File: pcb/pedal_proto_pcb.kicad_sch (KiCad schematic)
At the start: 18 parts, among them J1 100k_pot_1, J10 100k_pot_2, J11 250k_pot_1, J12 250k_pot_2, J13 stomp_b, J14 stomp_a, J15 stomp_c, J16 switch, J17 LED, J18 LED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

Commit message: feat: pcb done
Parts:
- removed J10: 100k_pot_2, symbol Connector:Conn_01x03_Socket
- removed J11: 250k_pot_1, symbol Connector:Conn_01x03_Socket
- removed J12: 250k_pot_2, symbol Connector:Conn_01x03_Socket
- removed J13: stomp_b, symbol Connector:Conn_01x03_Socket
- removed J14: stomp_a, symbol Connector:Conn_01x03_Socket
- removed J15: stomp_c, symbol Connector:Conn_01x03_Socket
- removed J16: switch, symbol Connector:Conn_01x03_Socket
- removed J9: 100k_pot_1, symbol Connector:Conn_01x03_Socket
- added J10: 100k_pot_1_B, Connector_PinHeader_2.54mm:PinHeader_1x02_P2.54mm_Vertical, symbol Connector:Conn_01x02_Socket
- added J11: 100k_pot_1_C, Connector_PinHeader_2.54mm:PinHeader_1x02_P2.54mm_Vertical, symbol Connector:Conn_01x02_Socket
- added J12: 100k_pot_2_A, Connector_PinHeader_2.54mm:PinHeader_1x02_P2.54mm_Vertical, symbol Connector:Conn_01x02_Socket
- added J13: 100k_pot_2_B, Connector_PinHeader_2.54mm:PinHeader_1x02_P2.54mm_Vertical, symbol Connector:Conn_01x02_Socket
- added J14: 100k_pot_2_C, Connector_PinHeader_2.54mm:PinHeader_1x02_P2.54mm_Vertical, symbol Connector:Conn_01x02_Socket
- added J15: 250k_pot_1_A, Connector_PinHeader_2.54mm:PinHeader_1x02_P2.54mm_Vertical, symbol Connector:Conn_01x02_Socket
- added J16: 250k_pot_1_B, Connector_PinHeader_2.54mm:PinHeader_1x02_P2.54mm_Vertical, symbol Connector:Conn_01x02_Socket
- added J19: 250k_pot_2_B, Connector_PinHeader_2.54mm:PinHeader_1x02_P2.54mm_Vertical, symbol Connector:Conn_01x02_Socket
- added J20: 250k_pot_2_C, Connector_PinHeader_2.54mm:PinHeader_1x02_P2.54mm_Vertical, symbol Connector:Conn_01x02_Socket
- added J21: stomp_1_A, Connector_PinHeader_2.54mm:PinHeader_1x02_P2.54mm_Vertical, symbol Connector:Conn_01x02_Socket
- added J22: stomp_1_B, Connector_PinHeader_2.54mm:PinHeader_1x02_P2.54mm_Vertical, symbol Connector:Conn_01x02_Socket
- added J23: stomp_1_C, Connector_PinHeader_2.54mm:PinHeader_1x02_P2.54mm_Vertical, symbol Connector:Conn_01x02_Socket
- added J24: stomp_2_A, Connector_PinHeader_2.54mm:PinHeader_1x02_P2.54mm_Vertical, symbol Connector:Conn_01x02_Socket
- added J25: stomp_2_B, Connector_PinHeader_2.54mm:PinHeader_1x02_P2.54mm_Vertical, symbol Connector:Conn_01x02_Socket
- added J26, J29: stomp_2_C, Connector_PinHeader_2.54mm:PinHeader_1x02_P2.54mm_Vertical, symbol Connector:Conn_01x02_Socket
- added J27: stomp_3_A, Connector_PinHeader_2.54mm:PinHeader_1x02_P2.54mm_Vertical, symbol Connector:Conn_01x02_Socket
- added J28: stomp_3_B, Connector_PinHeader_2.54mm:PinHeader_1x02_P2.54mm_Vertical, symbol Connector:Conn_01x02_Socket
- added J30: switch_A, Connector_PinHeader_2.54mm:PinHeader_1x02_P2.54mm_Vertical, symbol Connector:Conn_01x02_Socket
- added J31: switch_B, Connector_PinHeader_2.54mm:PinHeader_1x02_P2.54mm_Vertical, symbol Connector:Conn_01x02_Socket
- added J32: switch_C, Connector_PinHeader_2.54mm:PinHeader_1x02_P2.54mm_Vertical, symbol Connector:Conn_01x02_Socket
- added J33: GND, Connector_PinHeader_2.54mm:PinHeader_1x02_P2.54mm_Vertical, symbol Connector:Conn_01x02_Socket
- added J34: VDD, Connector_PinHeader_2.54mm:PinHeader_1x02_P2.54mm_Vertical, symbol Connector:Conn_01x02_Socket
- added J35: LED-, Connector_PinHeader_2.54mm:PinHeader_1x02_P2.54mm_Vertical, symbol Connector:Conn_01x02_Socket
- added J36: LED+, Connector_PinHeader_2.54mm:PinHeader_1x02_P2.54mm_Vertical, symbol Connector:Conn_01x02_Socket
- added J9: 100k_pot_1_A, Connector_PinHeader_2.54mm:PinHeader_1x02_P2.54mm_Vertical, symbol Connector:Conn_01x02_Socket
- J1, J2, J3, J4, J6: footprint (none) -> Connector_PinHeader_2.54mm:PinHeader_1x04_P2.54mm_Vertical
- J17: value LED -> 250k_pot_1_C; footprint (none) -> Connector_PinHeader_2.54mm:PinHeader_1x02_P2.54mm_Vertical
- J18: value LED -> 250k_pot_2_A; footprint (none) -> Connector_PinHeader_2.54mm:PinHeader_1x02_P2.54mm_Vertical
- J5: footprint (none) -> Connector_PinHeader_2.54mm:PinHeader_1x10_P2.54mm_Vertical
- J7, J8: footprint (none) -> Connector_PinHeader_2.54mm:PinHeader_1x02_P2.54mm_Vertical
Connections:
- net 0: now also J33.1 (Pin_1), J33.2 (Pin_2); no longer J18.1 (Pin_1)
- net VDD: now also J34.1 (Pin_1), J34.2 (Pin_2); no longer J18.2 (Pin_2)
- net at J6.2 (Pin_2): now also J30.1 (Pin_1), J30.2 (Pin_2)
- net at J6.3 (Pin_3): now also J31.1 (Pin_1), J31.2 (Pin_2)
- net at J6.4 (Pin_4): now also J32.1 (Pin_1), J32.2 (Pin_2)
- net at J5.5 (Pin_5): now also J24.1 (Pin_1), J24.2 (Pin_2)
- net at J5.6 (Pin_6): now also J25.1 (Pin_1), J25.2 (Pin_2)
- net at J5.7 (Pin_7): now also J26.1 (Pin_1), J26.2 (Pin_2)
- net at J2.2 (Pin_2): now also J12.1 (Pin_1), J12.2 (Pin_2)
- net at J2.3 (Pin_3): now also J13.1 (Pin_1), J13.2 (Pin_2)
- net at J2.4 (Pin_4): now also J14.1 (Pin_1), J14.2 (Pin_2)
- net at J5.10 (Pin_10): now also J29.1 (Pin_1), J29.2 (Pin_2)
- net at J5.2 (Pin_2): now also J21.1 (Pin_1), J21.2 (Pin_2)
- net at J5.3 (Pin_3): now also J22.1 (Pin_1), J22.2 (Pin_2)
- net at J5.4 (Pin_4): now also J23.1 (Pin_1), J23.2 (Pin_2)
- net at J5.8 (Pin_8): now also J27.1 (Pin_1), J27.2 (Pin_2)
- net at J5.9 (Pin_9): now also J28.1 (Pin_1), J28.2 (Pin_2)
- net at J1.2 (Pin_2): now also J9.1 (Pin_1), J9.2 (Pin_2)
- net at J1.3 (Pin_3): now also J10.1 (Pin_1), J10.2 (Pin_2)
- net at J1.4 (Pin_4): now also J11.1 (Pin_1), J11.2 (Pin_2)
- net at J4.2 (Pin_2): now also J18.1 (Pin_1), J18.2 (Pin_2)
- net at J4.3 (Pin_3): now also J19.1 (Pin_1), J19.2 (Pin_2)
- net at J4.4 (Pin_4): now also J20.1 (Pin_1), J20.2 (Pin_2)
- net at J3.2 (Pin_2): now also J15.1 (Pin_1), J15.2 (Pin_2)
- net at J3.3 (Pin_3): now also J16.1 (Pin_1), J16.2 (Pin_2)
- net at J3.4 (Pin_4): now also J17.1 (Pin_1), J17.2 (Pin_2)
- net at J8.1 (Pin_1): now also J35.1 (Pin_1), J35.2 (Pin_2); no longer J17.1 (Pin_1)
- net at J8.2 (Pin_2): now also J36.1 (Pin_1), J36.2 (Pin_2); no longer J17.2 (Pin_2)
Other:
- moved on the sheet: J1, J2, J3, J4, J5, J6, J7, J8

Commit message: feat: updated pcb
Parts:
- removed J1: 100k_pot_1, Connector_PinHeader_2.54mm:PinHeader_1x04_P2.54mm_Vertical, symbol Connector:Conn_01x04_Socket
- removed J2: 100k_pot_2, Connector_PinHeader_2.54mm:PinHeader_1x04_P2.54mm_Vertical, symbol Connector:Conn_01x04_Socket
- removed J3: 250k_pot_1, Connector_PinHeader_2.54mm:PinHeader_1x04_P2.54mm_Vertical, symbol Connector:Conn_01x04_Socket
- removed J4: 250k_pot_2, Connector_PinHeader_2.54mm:PinHeader_1x04_P2.54mm_Vertical, symbol Connector:Conn_01x04_Socket
- removed J5: stomp, Connector_PinHeader_2.54mm:PinHeader_1x10_P2.54mm_Vertical, symbol Connector:Conn_01x10_Socket
- removed J6: switch, Connector_PinHeader_2.54mm:PinHeader_1x04_P2.54mm_Vertical, symbol Connector:Conn_01x04_Socket
- removed J7: power, Connector_PinHeader_2.54mm:PinHeader_1x02_P2.54mm_Vertical, symbol Connector:Conn_01x02_Socket
- removed J8: LED, Connector_PinHeader_2.54mm:PinHeader_1x02_P2.54mm_Vertical, symbol Connector:Conn_01x02_Socket
- added D1: LED, LED_THT:LED_D4.0mm, symbol Device:LED
- added J1, J2, J3, J37, J4, J8: GND, Connector_PinHeader_2.54mm:PinHeader_1x01_P2.54mm_Vertical, symbol Connector:Conn_01x01_Socket
- added J38: input, Connector_PinHeader_2.54mm:PinHeader_1x02_P2.54mm_Vertical, symbol Connector:Conn_01x02_Socket
- added J39: output, Connector_PinHeader_2.54mm:PinHeader_1x02_P2.54mm_Vertical, symbol Connector:Conn_01x02_Socket
- added J5: Jack-DC, Additional_Connectors:Barrel_Plug_5.5mmx2.1mm, symbol Connector:Jack-DC
- added J6: Barrel_Jack_Output, Connector_PinHeader_2.54mm:PinHeader_1x02_P2.54mm_Vertical, symbol Connector:Barrel_Jack
- added J7: Barrel_Jack_Input, Connector_PinHeader_2.54mm:PinHeader_1x02_P2.54mm_Vertical, symbol Connector:Barrel_Jack
- added RV1, RV2: 100k_Potentiometer, Additional_Switches:Lug_Pot, symbol Device:R_Potentiometer
- added RV3, RV4: 250k_Potentiometer, Additional_Switches:Lug_Pot, symbol Device:R_Potentiometer
- added SW1: SW_3PDT, Additional_Switches:3PDT, symbol Additional_Switches:3PDT
- added SW2: SW_SPDT, Additional_Switches:SPDT, symbol Switch:SW_SPDT
- J10: value 100k_pot_1_B -> RV1_2
- J11: value 100k_pot_1_C -> RV1_1
- J12: value 100k_pot_2_A -> RV2_3
- J13: value 100k_pot_2_B -> RV2_2
- J14: value 100k_pot_2_C -> RV2_1
- J15: value 250k_pot_1_A -> RV3_3
- J16: value 250k_pot_1_B -> RV3_2
- J17: value 250k_pot_1_C -> RV3_1
- J18: value 250k_pot_2_A -> RV4_3
- J19: value 250k_pot_2_B -> RV4_2
- J20: value 250k_pot_2_C -> RV4_1
- J21: value stomp_1_A -> stomp_A_1
- J22: value stomp_1_B -> stomp_A_2
- J23: value stomp_1_C -> stomp_A_3
- J24: value stomp_2_A -> stomp_B_1
- J25: value stomp_2_B -> stomp_B_2
- J26: value stomp_2_C -> stomp_B_3
- J27: value stomp_3_A -> stomp_C_1
- J28: value stomp_3_B -> stomp_C_2
- J29: value stomp_2_C -> stomp_C_3
- J30: value switch_A -> switch_1
- J31: value switch_B -> switch_2
- J32: value switch_C -> switch_3
- J9: value 100k_pot_1_A -> RV1_3
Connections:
- net 0: now also J1.1 (Pin_1), J2.1 (Pin_1), J3.1 (Pin_1), J37.1 (Pin_1), J4.1 (Pin_1), J5.2, J6.1, J7.1, J8.1 (Pin_1)
- net at J14.1 (Pin_1), J14.2 (Pin_2): now also RV2.1
- net at J18.1 (Pin_1), J18.2 (Pin_2): now also RV4.3
- net at J22.1 (Pin_1), J22.2 (Pin_2): now also SW1.2 (A2)
- net at J16.1 (Pin_1), J16.2 (Pin_2): now also RV3.2
- net at J25.1 (Pin_1), J25.2 (Pin_2): now also SW1.5 (B2)
- net at J29.1 (Pin_1), J29.2 (Pin_2): now also SW1.9 (C3)
- net at J28.1 (Pin_1), J28.2 (Pin_2): now also SW1.8 (C2)
- net at J9.1 (Pin_1), J9.2 (Pin_2): now also RV1.3
- net at J21.1 (Pin_1), J21.2 (Pin_2): now also SW1.1 (A1)
- net at J23.1 (Pin_1), J23.2 (Pin_2): now also SW1.3 (A3)
- net at J24.1 (Pin_1), J24.2 (Pin_2): now also SW1.4 (B1)
- net at J26.1 (Pin_1), J26.2 (Pin_2): now also SW1.6 (B3)
- net at J27.1 (Pin_1), J27.2 (Pin_2): now also SW1.7 (C1)
- net at J32.1 (Pin_1), J32.2 (Pin_2): now also SW2.3 (C)
- net at J30.1 (Pin_1), J30.2 (Pin_2): now also SW2.1 (A)
- net at J19.1 (Pin_1), J19.2 (Pin_2): now also RV4.2
- net at J17.1 (Pin_1), J17.2 (Pin_2): now also RV3.1
- net at J20.1 (Pin_1), J20.2 (Pin_2): now also RV4.1
- net at J31.1 (Pin_1), J31.2 (Pin_2): now also SW2.2 (B)
- net at J10.1 (Pin_1), J10.2 (Pin_2): now also RV1.2
- net at J35.1 (Pin_1), J35.2 (Pin_2): now also D1.1 (K)
- net at J36.1 (Pin_1), J36.2 (Pin_2): now also D1.2 (A)
- net at J15.1 (Pin_1), J15.2 (Pin_2): now also RV3.3
- net at J12.1 (Pin_1), J12.2 (Pin_2): now also RV2.3
- net at J13.1 (Pin_1), J13.2 (Pin_2): now also RV2.2
- net at J11.1 (Pin_1), J11.2 (Pin_2): now also RV1.1
- net VDD: no longer names the net of J34.1 (Pin_1), J34.2 (Pin_2)
- net VDD: now also J5.1
- new net: J39.1 (Pin_1), J39.2 (Pin_2), J6.2
- new net: J38.1 (Pin_1), J38.2 (Pin_2), J7.2
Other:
- moved on the sheet: J10, J11, J12, J13, J14, J15, J16, J17, J18, J19, J20, J21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

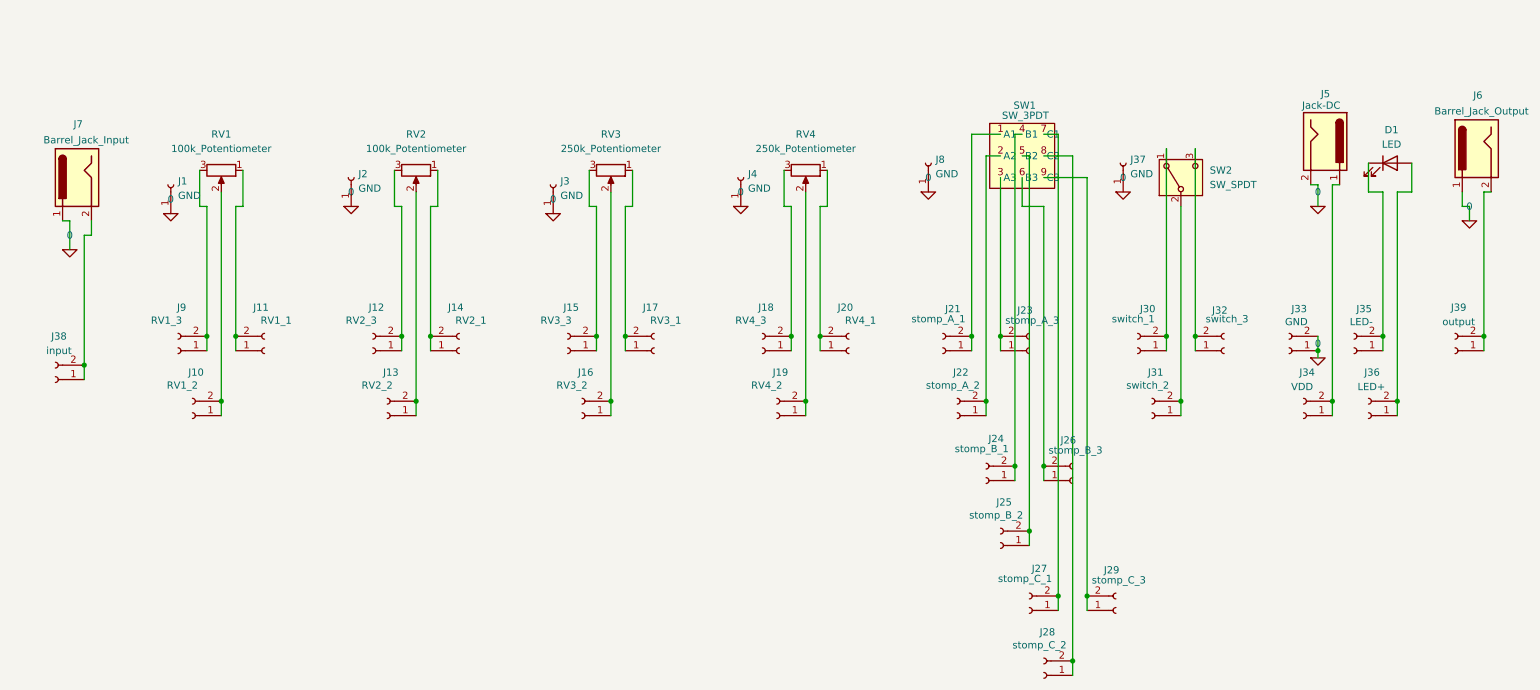
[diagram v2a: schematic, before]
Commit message: feat: added GND, pwr led and prw switch
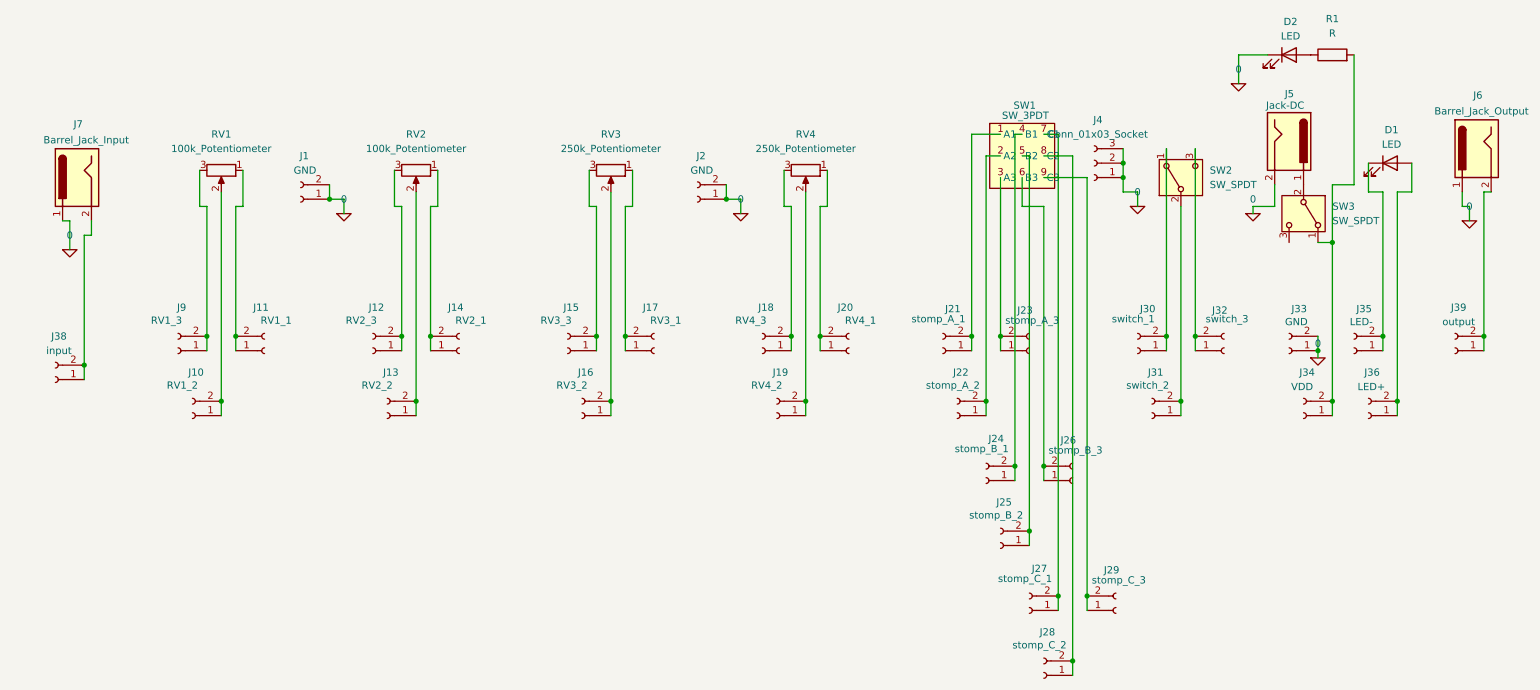
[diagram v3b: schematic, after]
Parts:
- removed J1, J2, J3, J37, J4, J8: GND, Connector_PinHeader_2.54mm:PinHeader_1x01_P2.54mm_Vertical, symbol Connector:Conn_01x01_Socket
- added D2: LED, LED_THT:LED_D4.0mm, symbol Device:LED
- added J1, J2: GND, Connector_PinHeader_2.54mm:PinHeader_1x02_P2.54mm_Vertical, symbol Connector:Conn_01x02_Socket
- added J4: Conn_01x03_Socket, Connector_PinHeader_2.54mm:PinHeader_1x03_P2.54mm_Vertical, symbol Connector:Conn_01x03_Socket
- added R1: R, Resistor_THT:R_Axial_DIN0204_L3.6mm_D1.6mm_P7.62mm_Horizontal, symbol Device:R
- added SW3: SW_SPDT, Additional_Switches:SPDT, symbol Switch:SW_SPDT
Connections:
- net 0: now also D2.1 (K), J1.1 (Pin_1), J1.2 (Pin_2), J2.1 (Pin_1), J2.2 (Pin_2), J4.1 (Pin_1), J4.2 (Pin_2), J4.3 (Pin_3)
- net at J34.1 (Pin_1), J34.2 (Pin_2): now also R1.2, SW3.1 (A); no longer J5.1
- new net: J5.1, SW3.2 (B)
- new net: D2.2 (A), R1.1
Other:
- moved on the sheet: J5

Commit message: feat: almost done
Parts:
- removed J1, J2: GND, Connector_PinHeader_2.54mm:PinHeader_1x02_P2.54mm_Vertical, symbol Connector:Conn_01x02_Socket
- removed J4: Conn_01x03_Socket, Connector_PinHeader_2.54mm:PinHeader_1x03_P2.54mm_Vertical, symbol Connector:Conn_01x03_Socket
- added J1, J2, J3, J37, J4, J40, J8: GND, Connector_PinHeader_2.54mm:PinHeader_1x01_P2.54mm_Vertical, symbol Connector:Conn_01x01_Socket
- added R2: 330, Resistor_THT:R_Axial_DIN0309_L9.0mm_D3.2mm_P12.70mm_Horizontal, symbol Device:R
- R1: value R -> 330; footprint Resistor_THT:R_Axial_DIN0204_L3.6mm_D1.6mm_P7.62mm_Horizontal -> Resistor_THT:R_Axial_DIN0309_L9.0mm_D3.2mm_P12.70mm_Horizontal
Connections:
- net 0: now also J1.1 (Pin_1), J2.1 (Pin_1), J3.1 (Pin_1), J37.1 (Pin_1), J4.1 (Pin_1), J40.1 (Pin_1), J8.1 (Pin_1)
- net at J36.1 (Pin_1), J36.2 (Pin_2): now also R2.1; no longer D1.2 (A)
- new net: D1.2 (A), R2.2
